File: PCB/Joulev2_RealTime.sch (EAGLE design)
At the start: 54 parts, among them J12_HEADER J12HEADER_(JOULE), Q1 BSS138, Q2 BSS138, Q3 BSS138, Q4 BSS138, Q5 BSS138, Q6 BSS138, Q7 BSS138, Q8 BSS138, U1 ATMEGA328P_TQFP, U2 RFM69CW, Y1 16MHz

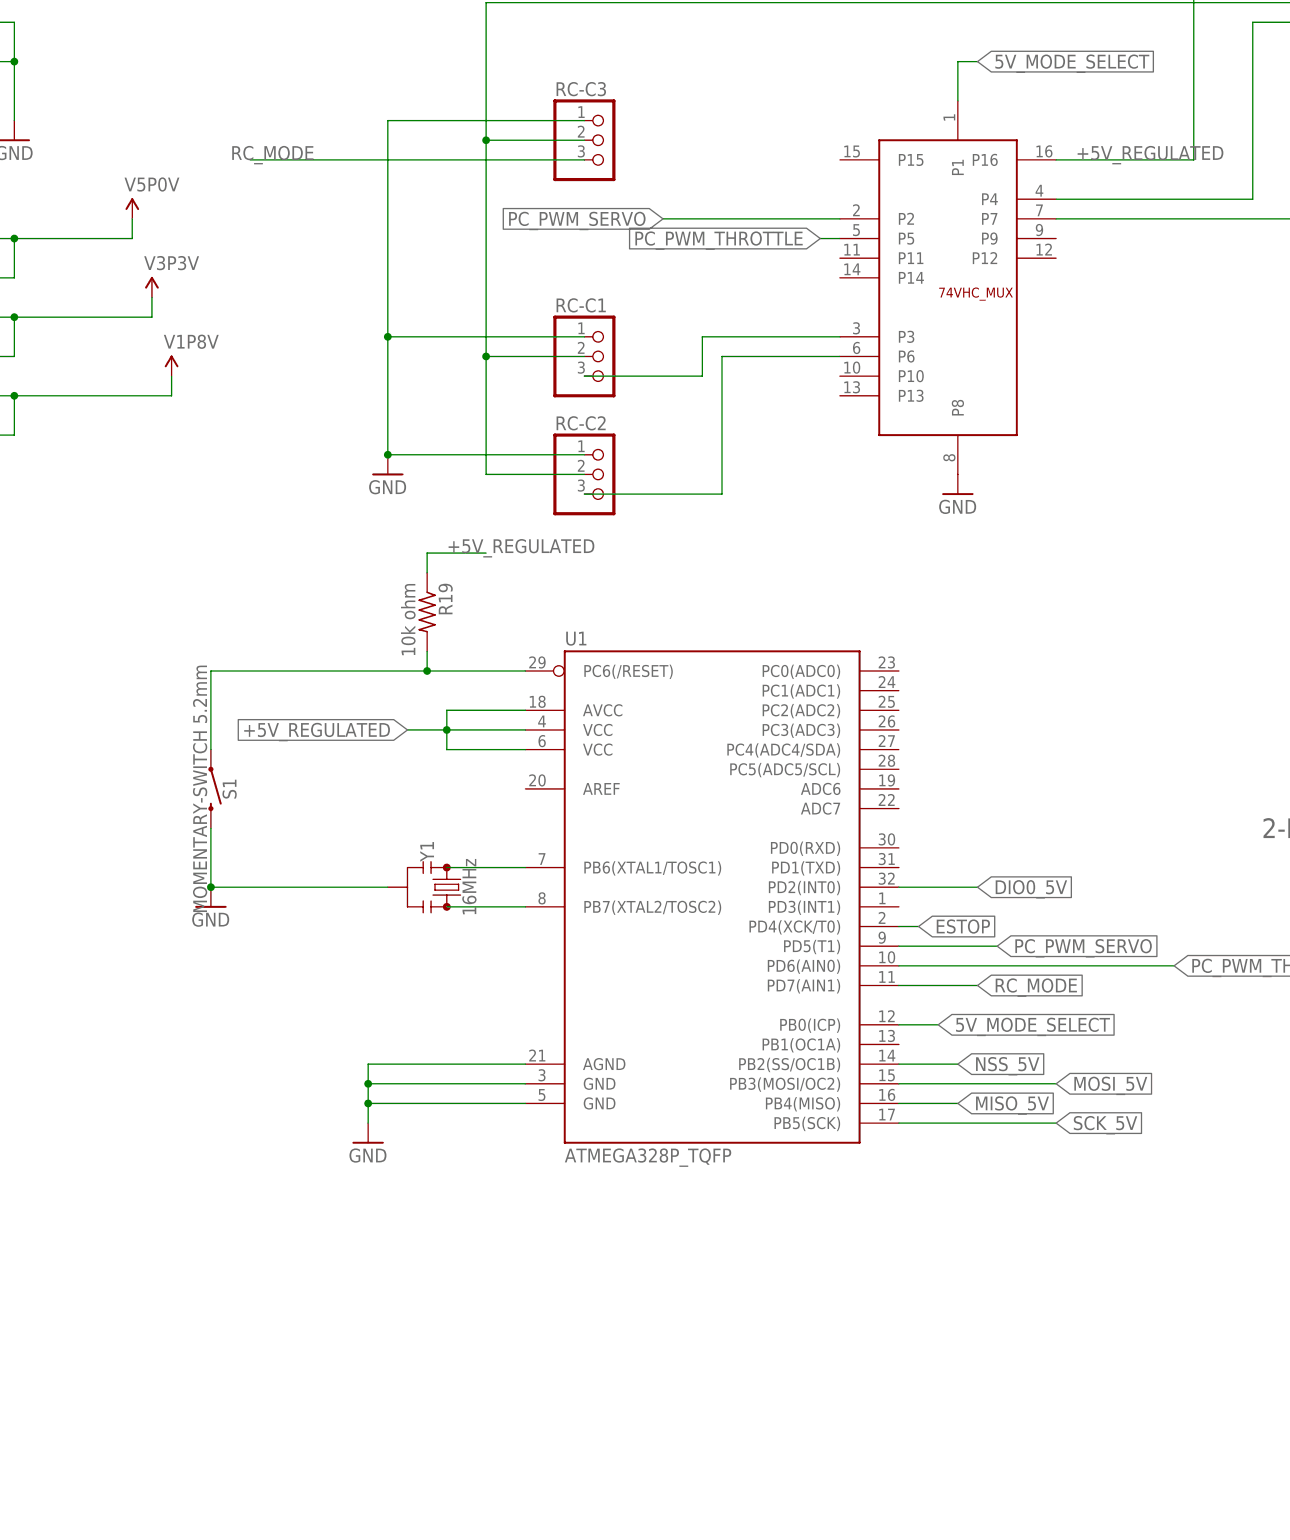
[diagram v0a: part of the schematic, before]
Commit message: Updated minor changes on old board. will now be using shield design.
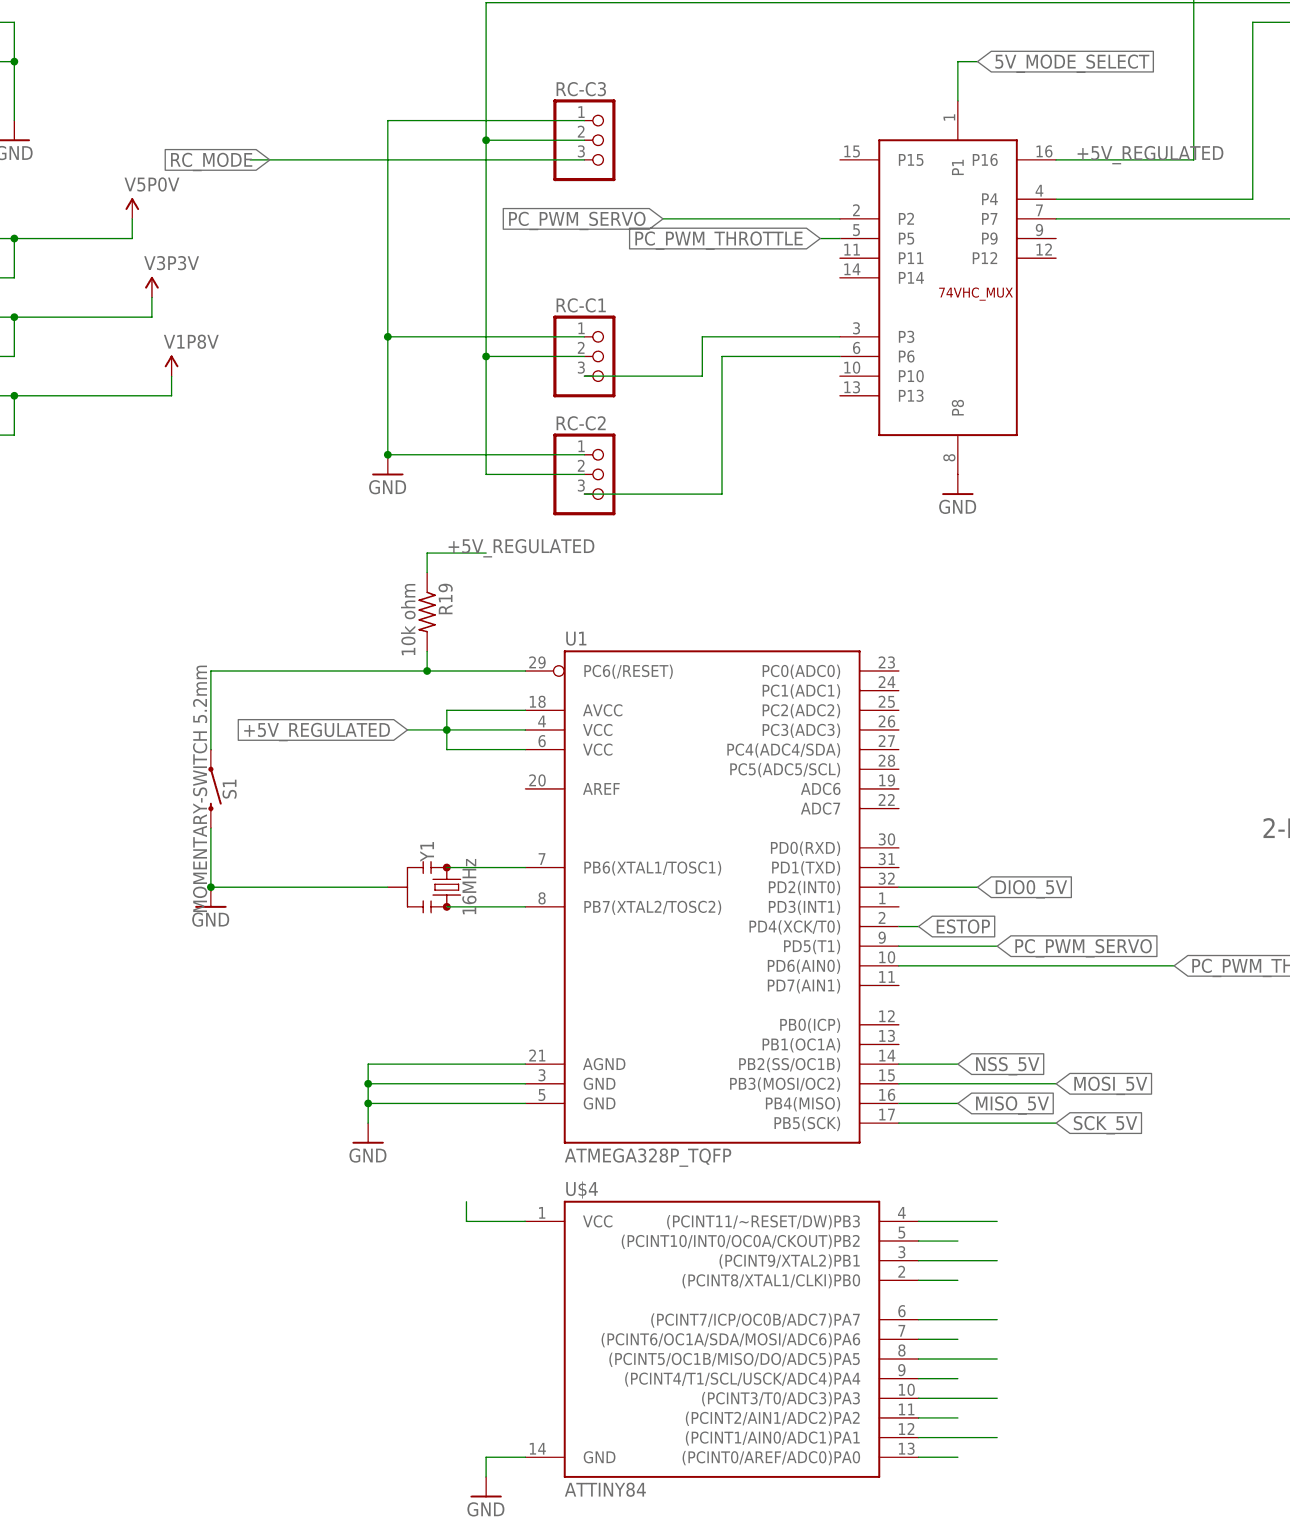
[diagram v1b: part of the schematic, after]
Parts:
- added U$4: ATTINY84, SparkFun-IC-Microcontroller:ATTINY84
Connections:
- new net N$12: U$4.(PCINT5/OC1B/MISO/DO/ADC5)PA5
- new net N$13: U$4.(PCINT7/ICP/OC0B/ADC7)PA7
- new net N$14: U$4.(PCINT4/T1/SCL/USCK/ADC4)PA4
- new net N$15: U$4.(PCINT3/T0/ADC3)PA3
- new net N$16: U$4.(PCINT2/AIN1/ADC2)PA2
- new net N$17: U$4.(PCINT1/AIN0/ADC1)PA1
- new net N$18: U$4.(PCINT0/AREF/ADC0)PA0
- new net N$19: U$4.(PCINT8/XTAL1/CLKI)PB0
- new net N$21: U$4.(PCINT9/XTAL2)PB1
- new net N$22: U$4.(PCINT10/INT0/OC0A/CKOUT)PB2
- new net N$23: U$4.(PCINT11/~RESET/DW)PB3
- new net N$24: U$4.VCC
- new net N$9: U$4.(PCINT6/OC1A/SDA/MOSI/ADC6)PA6
- net 5V_MODE_SELECT: no longer U1.PB0(ICP)
- net GND: now also U$4.GND
- net RC_MODE: no longer U1.PD7(AIN1)
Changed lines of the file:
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@@
 <?xml version="1.0" encoding="utf-8"?>
 <!DOCTYPE eagle SYSTEM "eagle.dtd">
-<eagle version="7.6.0">
+<eagle version="8.1.1">
 <drawing>
 <settings>
@@
 <layer number="2" name="Route2" color="1" fill="3" visible="no" active="no"/>
 <layer number="3" name="Route3" color="4" fill="3" visible="no" active="no"/>
+<layer number="4" name="Route4" color="1" fill="4" visible="no" active="no"/>
+<layer number="5" name="Route5" color="4" fill="4" visible="no" active="no"/>
+<layer number="6" name="Route6" color="1" fill="8" visible="no" active="no"/>
+<layer number="7" name="Route7" color="4" fill="8" visible="no" active="no"/>
+<layer number="8" name="Route8" color="1" fill="2" visible="no" active="no"/>
+<layer number="9" name="Route9" color="4" fill="2" visible="no" active="no"/>
+<layer number="10" name="Route10" color="1" fill="7" visible="no" active="no"/>
+<layer number="11" name="Route11" color="4" fill="7" visible="no" active="no"/>
+<layer number="12" name="Route12" color="1" fill="5" visible="no" active="no"/>
+<layer number="13" name="Route13" color="4" fill="5" visible="no" active="no"/>
 <layer number="14" name="Route14" color="1" fill="6" visible="no" active="no"/>
 <layer number="15" name="Route15" color="4" fill="6" visible="no" active="no"/>
@@
 <part name="VCC_COMP" library="SparkFun-Aesthetics" deviceset="VCC" device="" value="VCC_COMP"/>
 <part name="BARRELJACK" library="RoboJackets-Connectors" deviceset="2-PIN_2MM-*" device="V"/>
+<part name="U$4" library="SparkFun-IC-Microcontroller" deviceset="ATTINY84" device="" value="ATTINY84"/>
+<part name="GND17" library="SparkFun-Aesthetics" deviceset="GND" device=""/>
 </parts>
 <sheets>
@@
 <instance part="VCC_COMP" gate="G$1" x="215.9" y="35.56"/>
 <instance part="BARRELJACK" gate="G$1" x="195.58" y="27.94"/>
+<instance part="U$4" gate="G$1" x="55.88" y="-55.88"/>
+<instance part="GND17" gate="1" x="25.4" y="-76.2"/>
 </instances>
 <busses>
@@
 <junction x="215.9" y="25.4"/>
 </segment>
+<segment>
+<pinref part="U$4" gate="G$1" pin="GND"/>
+<wire x1="30.48" y1="-71.12" x2="25.4" y2="-71.12" width="0.1524" layer="91"/>
+<wire x1="25.4" y1="-71.12" x2="25.4" y2="-73.66" width="0.1524" layer="91"/>
+<pinref part="GND17" gate="1" pin="GND"/>
+</segment>
 </net>
 <net name="ESTOP_GATE" class="0">
@@
 <pinref part="RC-C3" gate="A" pin="3"/>
 <wire x1="38.1" y1="96.52" x2="-5.08" y2="96.52" width="0.1524" layer="91"/>
-<label x="-7.62" y="96.52" size="1.778" layer="95"/>
-</segment>
-<segment>
-<pinref part="U1" gate="U$1" pin="PD7(AIN1)"/>
-<wire x1="78.74" y1="-10.16" x2="88.9" y2="-10.16" width="0.1524" layer="91"/>
-<label x="88.9" y="-10.16" size="1.778" layer="95" font="vector" xref="yes"/>
+<label x="-2.54" y="96.52" size="1.778" layer="95" rot="R180" xref="yes"/>
 </segment>
 </net>
@@
 </net>
 <net name="5V_MODE_SELECT" class="0">
-<segment>
-<pinref part="U1" gate="U$1" pin="PB0(ICP)"/>
-<wire x1="78.74" y1="-15.24" x2="83.82" y2="-15.24" width="0.1524" layer="91"/>
-<label x="83.82" y="-15.24" size="1.778" layer="95" font="vector" xref="yes"/>
-</segment>
 <segment>
 <pinref part="U$2" gate="G$1" pin="P1"/>
@@
 </segment>
 </net>
+<net name="N$9" class="0">
+<segment>
+<pinref part="U$4" gate="G$1" pin="(PCINT6/OC1A/SDA/MOSI/ADC6)PA6"/>
+<wire x1="81.28" y1="-55.88" x2="86.36" y2="-55.88" width="0.1524" layer="91"/>
+</segment>
+</net>
+<net name="N$12" class="0">
+<segment>
+<pinref part="U$4" gate="G$1" pin="(PCINT5/OC1B/MISO/DO/ADC5)PA5"/>
+<wire x1="81.28" y1="-58.42" x2="91.44" y2="-58.42" width="0.1524" layer="91"/>
+</segment>
+</net>
+<net name="N$13" class="0">
+<segment>
+<pinref part="U$4" gate="G$1" pin="(PCINT7/ICP/OC0B/ADC7)PA7"/>
+<wire x1="81.28" y1="-53.34" x2="91.44" y2="-53.34" width="0.1524" layer="91"/>
+</segment>
+</net>
+<net name="N$14" class="0">
+<segment>
+<pinref part="U$4" gate="G$1" pin="(PCINT4/T1/SCL/USCK/ADC4)PA4"/>
+<wire x1="81.28" y1="-60.96" x2="86.36" y2="-60.96" width="0.1524" layer="91"/>
+</segment>
+</net>
+<net name="N$15" class="0">
+<segment>
+<pinref part="U$4" gate="G$1" pin="(PCINT3/T0/ADC3)PA3"/>
+<wire x1="81.28" y1="-63.5" x2="91.44" y2="-63.5" width="0.1524" layer="91"/>
+</segment>
+</net>
+<net name="N$16" class="0">
+<segment>
+<pinref part="U$4" gate="G$1" pin="(PCINT2/AIN1/ADC2)PA2"/>
+<wire x1="81.28" y1="-66.04" x2="86.36" y2="-66.04" width="0.1524" layer="91"/>
+</segment>
+</net>
+<net name="N$17" class="0">
+<segment>
+<pinref part="U$4" gate="G$1" pin="(PCINT1/AIN0/ADC1)PA1"/>
+<wire x1="81.28" y1="-68.58" x2="91.44" y2="-68.58" width="0.1524" layer="91"/>
+</segment>
+</net>
+<net name="N$18" class="0">
+<segment>
+<pinref part="U$4" gate="G$1" pin="(PCINT0/AREF/ADC0)PA0"/>
+<wire x1="81.28" y1="-71.12" x2="86.36" y2="-71.12" width="0.1524" layer="91"/>
+</segment>
+</net>
+<net name="N$19" class="0">
+<segment>
+<pinref part="U$4" gate="G$1" pin="(PCINT8/XTAL1/CLKI)PB0"/>
+<wire x1="81.28" y1="-48.26" x2="86.36" y2="-48.26" width="0.1524" layer="91"/>
+</segment>
+</net>
+<net name="N$21" class="0">
+<segment>
+<pinref part="U$4" gate="G$1" pin="(PCINT9/XTAL2)PB1"/>
+<wire x1="81.28" y1="-45.72" x2="91.44" y2="-45.72" width="0.1524" layer="91"/>
+</segment>
+</net>
+<net name="N$22" class="0">
+<segment>
+<pinref part="U$4" gate="G$1" pin="(PCINT10/INT0/OC0A/CKOUT)PB2"/>
+<wire x1="81.28" y1="-43.18" x2="86.36" y2="-43.18" width="0.1524" layer="91"/>
+</segment>
+</net>
+<net name="N$23" class="0">
+<segment>
+<pinref part="U$4" gate="G$1" pin="(PCINT11/~RESET/DW)PB3"/>
+<wire x1="81.28" y1="-40.64" x2="91.44" y2="-40.64" width="0.1524" layer="91"/>
+</segment>
+</net>
+<net name="N$24" class="0">
+<segment>
+<pinref part="U$4" gate="G$1" pin="VCC"/>
+<wire x1="30.48" y1="-40.64" x2="22.86" y2="-40.64" width="0.1524" layer="91"/>
+<wire x1="22.86" y1="-40.64" x2="22.86" y2="-38.1" width="0.1524" layer="91"/>
+</segment>
+</net>
